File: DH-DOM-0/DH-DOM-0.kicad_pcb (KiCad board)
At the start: 2 copper layers, 40 x 40 mm, 44 parts, among them J1 USB_C_Receptacle_USB2.0_14P, J2 Conn_01x02, SW1 RST, SW2 BOOT, U3 LSM6DSOXTR, U4 MMC5983MA, U5 NCP1117-3.3_SOT223, U6 TVS1400DRV, U7 ESP32-S3-WROOM-1-N16R8, U8 TP4057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

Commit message: edit
added diode again? idk something happened
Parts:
- added Q1: FDN340P, Package_TO_SOT_SMD:SOT-23, F.Cu at (137.7, 115.0)
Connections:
- C15 pad 1: +5V -> /BAT+
- J2 pad 1: +5V -> /BAT+
- U8 pad 3: +5V -> /BAT+
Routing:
- net /BAT+: track 0.00 -> 26.3 mm
- net +5V: track 49.4 -> 54.2 mm

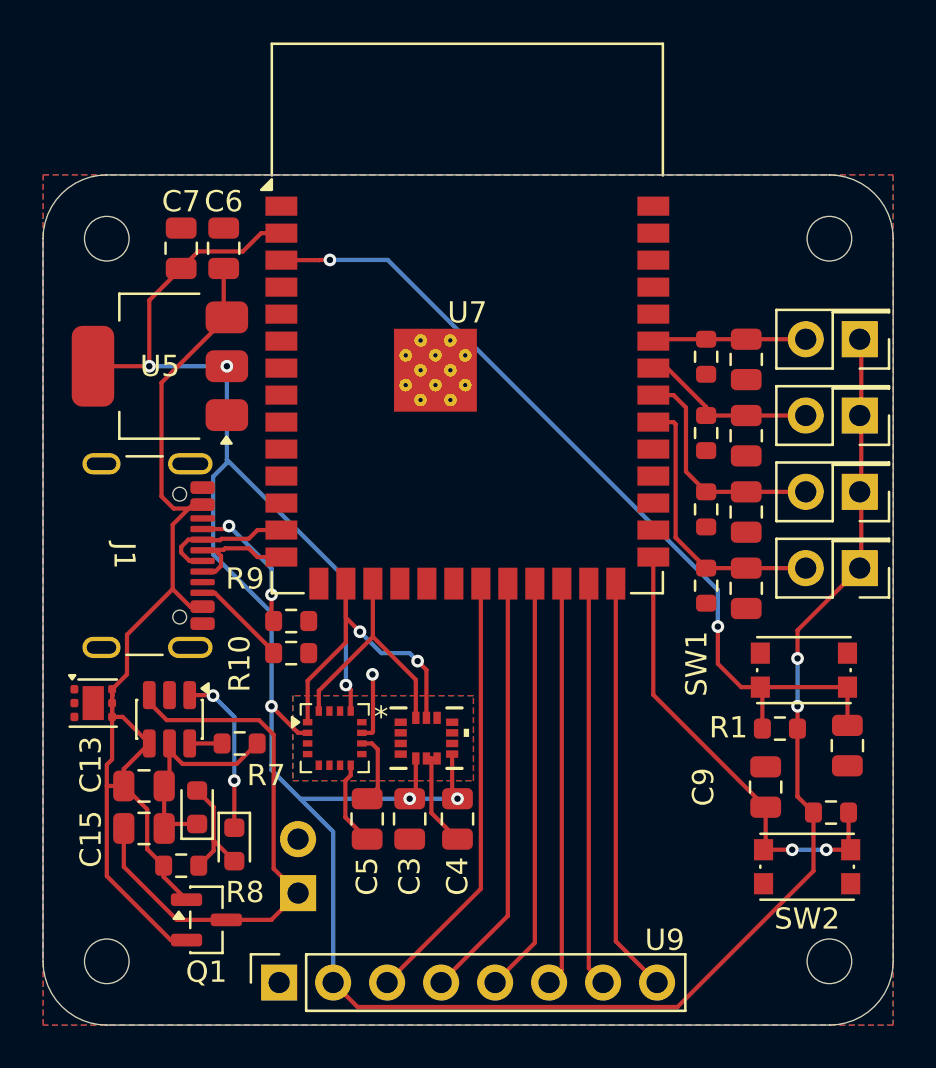
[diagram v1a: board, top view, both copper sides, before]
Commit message: fix
rerouted misrouted boot settings pins
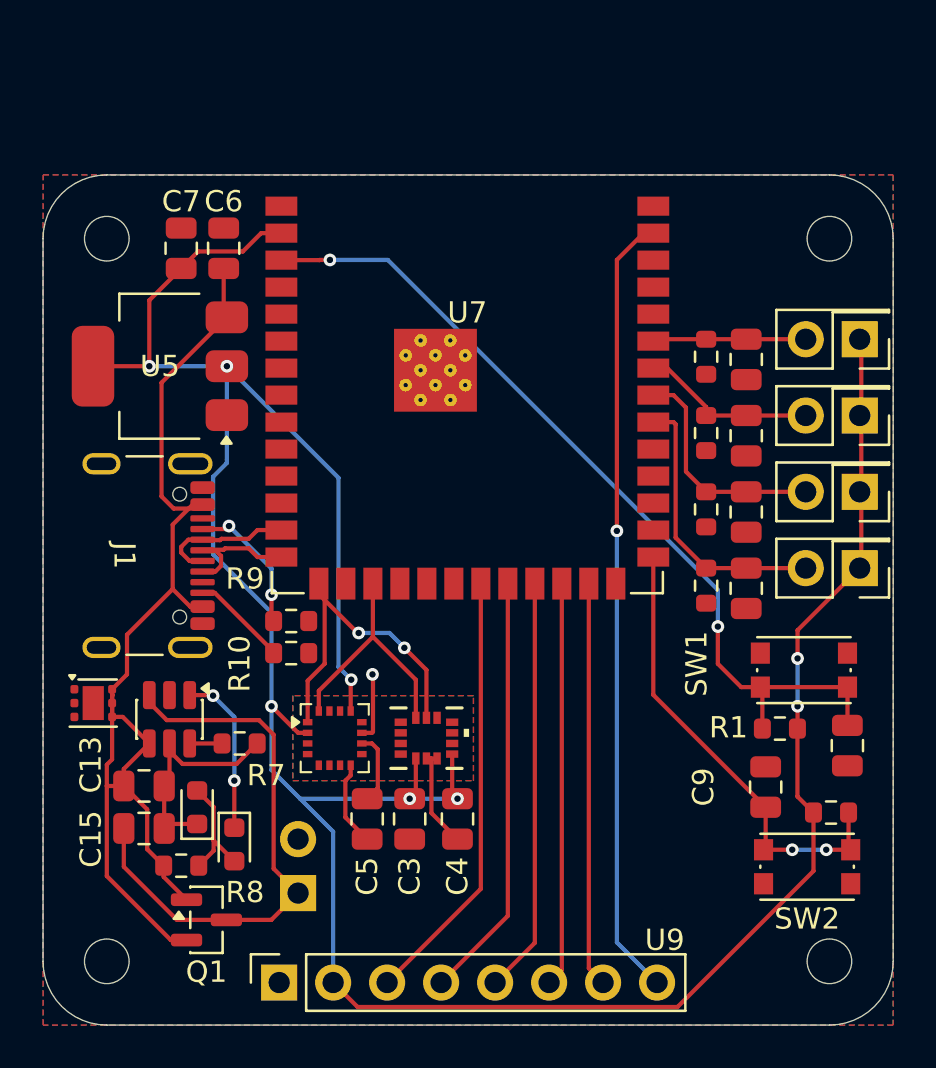
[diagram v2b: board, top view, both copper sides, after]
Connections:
- U7 pad 15: unconnected-(U7-IO3-Pad15) -> /SCL
- U7 pad 16: /SCL -> unconnected-(U7-IO46-Pad16)
- U7 pad 26: /BACKLIGHT -> unconnected-(U7-IO45-Pad26)
- U7 pad 39: unconnected-(U7-IO1-Pad39) -> /BACKLIGHT
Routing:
- net /BACKLIGHT: track 19.6 -> 37.0 mm, vias 0 -> 1
- net +3V3: track 128.9 -> 133.4 mm
- net /SCL: track 15.9 -> 16.5 mm

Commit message: edit
added bmi270 backup just in case LSM6DSOXTR goes out of stock (only 2 left)
might switch to another imu idk, ESP32 I2C library is a must.

Currently building BOM
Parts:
- U7: value ESP32-S3-WROOM-1-N16R8 -> ESP32-S3-WROOM-1-N4R8
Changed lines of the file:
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@@
 			)
 		)
-		(property "Value" "ESP32-S3-WROOM-1-N16R8"
+		(property "Value" "ESP32-S3-WROOM-1-N4R8"
 			(at 0 14.6 0)
 			(unlocked yes)
@@
 			(net "unconnected-(U7-IO15-Pad8)")
 			(pinfunction "IO15_8")
-			(pintype "bidirectional")
+			(pintype "bidirectional+no_connect")
 		)
 		(pad "9" smd rect
